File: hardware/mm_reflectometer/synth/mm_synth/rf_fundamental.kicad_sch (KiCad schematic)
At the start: 7 parts

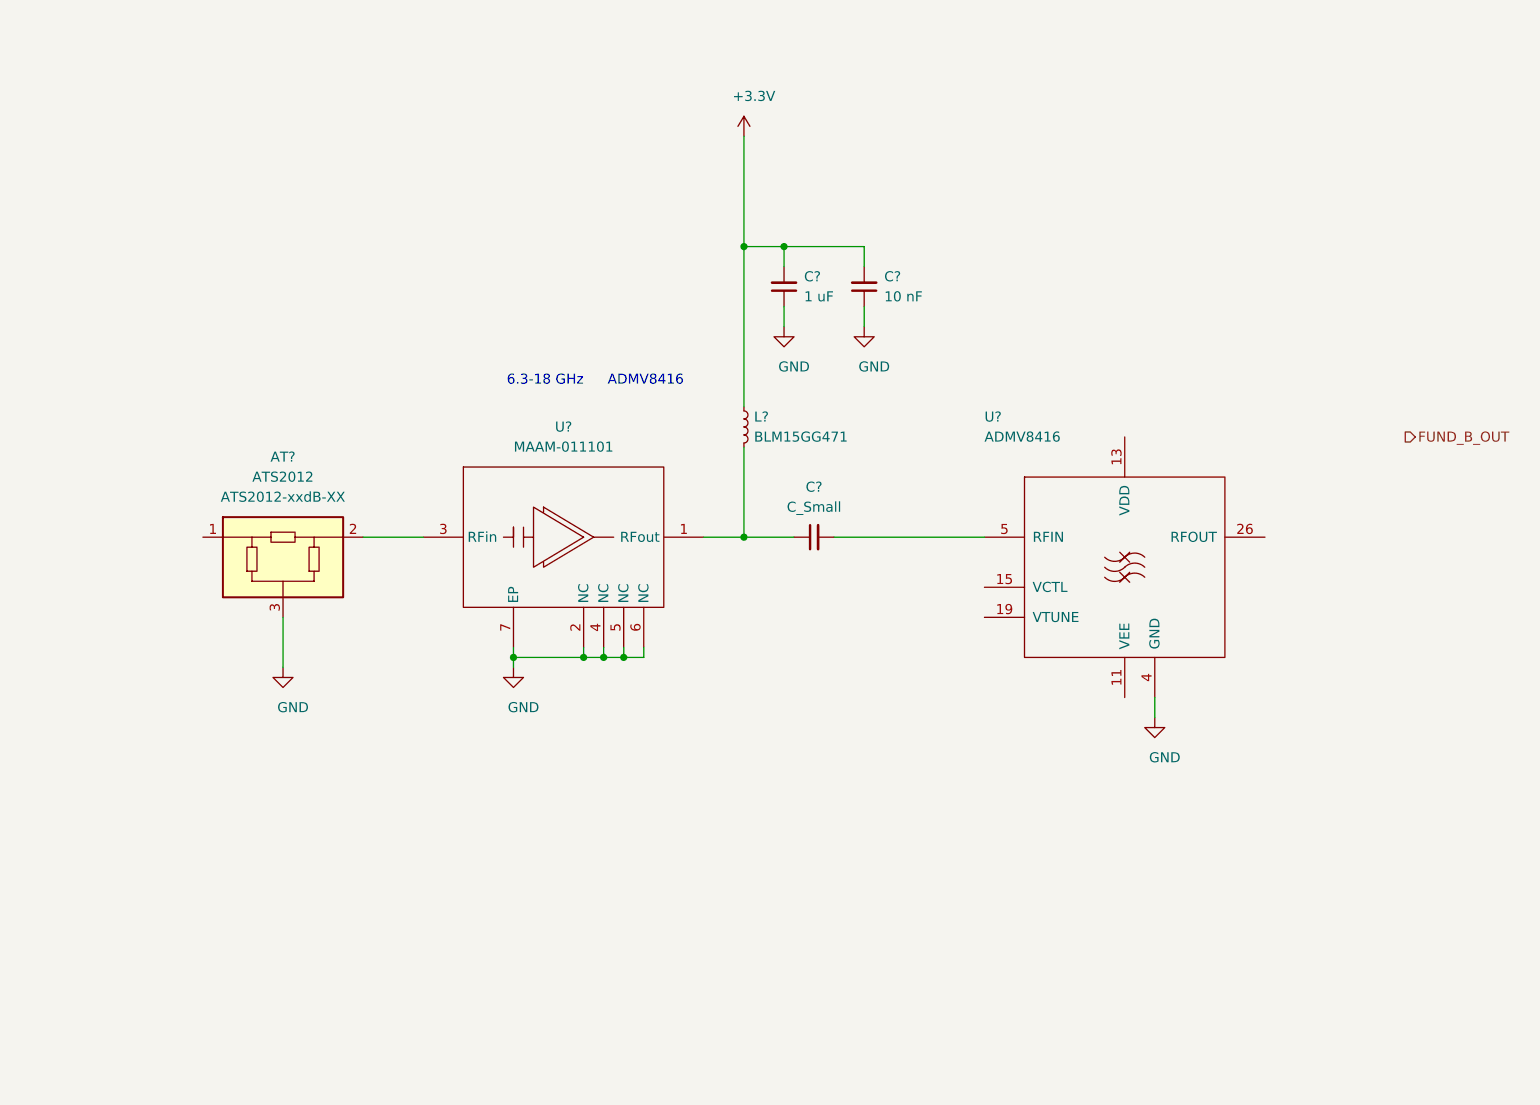
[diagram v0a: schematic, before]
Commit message: adding bias circuitry to mm synth
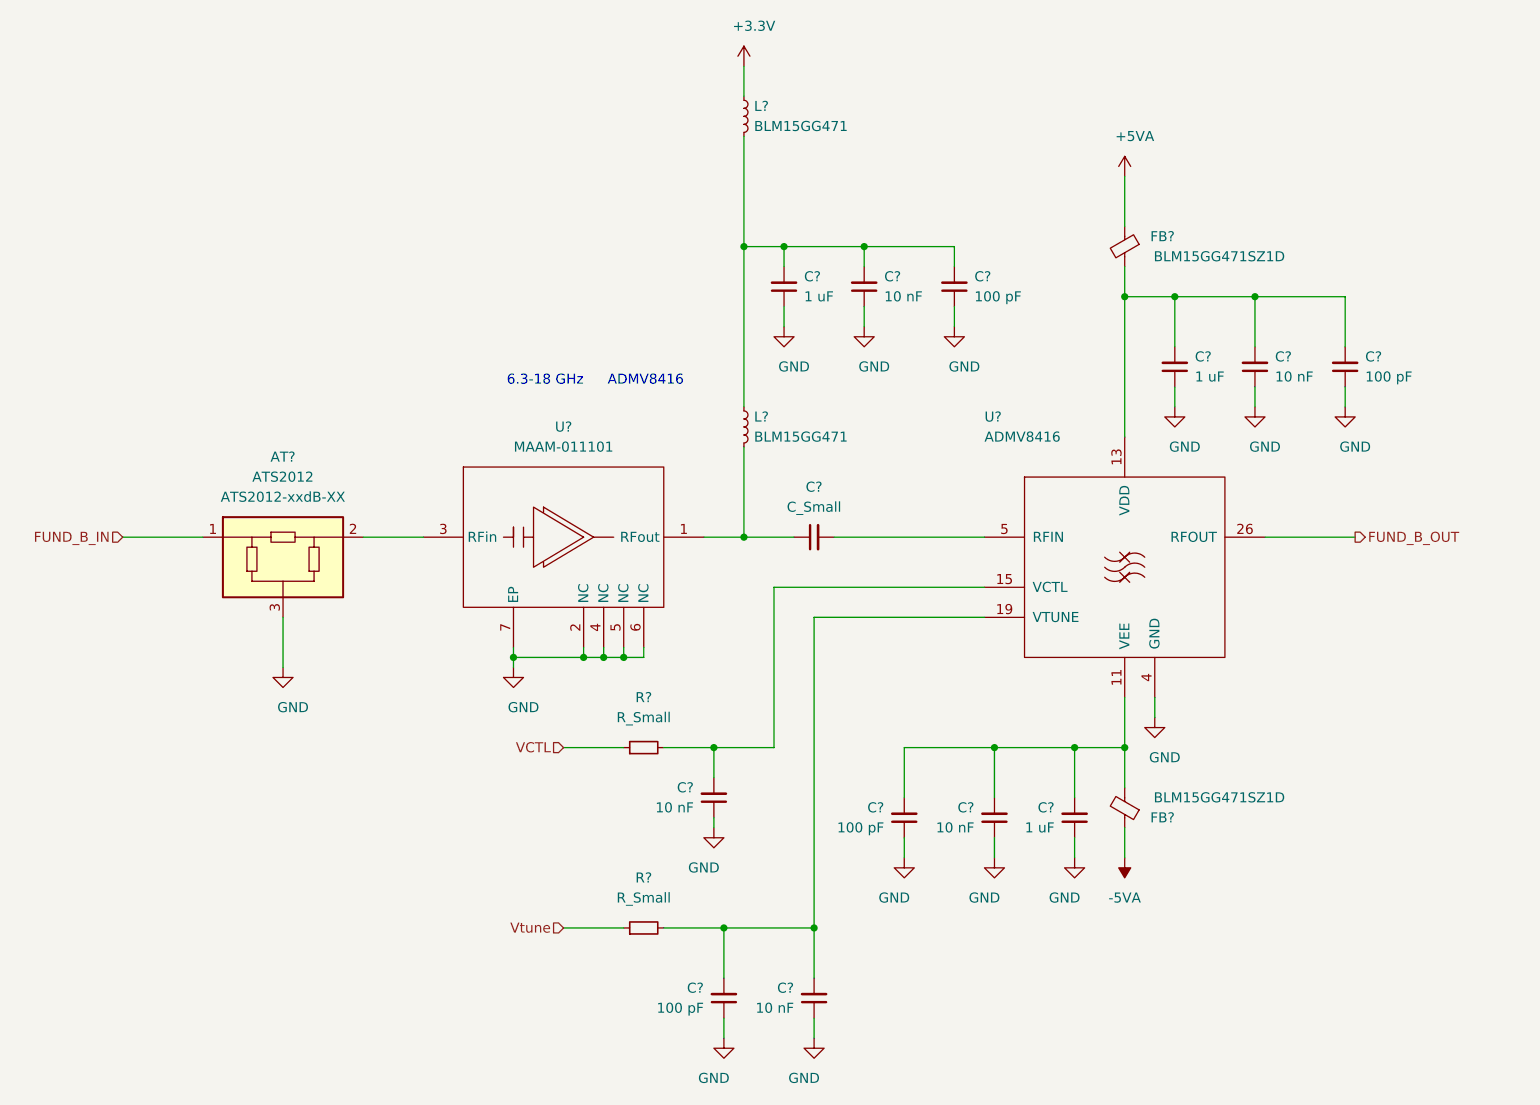
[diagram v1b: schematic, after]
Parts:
- added C? (x4): 10 nF, symbol Device:C_Small
- added C? (x4): 100 pF, symbol Device:C_Small
- added C? (x2): 1 uF, symbol Device:C_Small
- added FB? (x2): BLM15GG471SZ1D, symbol Device:FerriteBead_Small
- added L?: BLM15GG471, symbol Device:L_Small
- added R? (x2): R_Small, symbol Device:R_Small
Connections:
- net +3V3: now also L?.1; no longer C?.2, C?.2, L?.1
- net FUND_B_OUT: now also U?.26 (RFOUT)
- net GND: now also C?.1, C?.1, C?.1, C?.1, C?.1, C?.1, C?.1, C?.1, C?.1, C?.1
- net at U?.11 (VEE): now also C?.2, C?.2, C?.2, FB?.2
- net at U?.13 (VDD): now also C?.2, C?.2, C?.2, FB?.2
- net at U?.15 (VCTL): now also C?.2, R?.2
- net at U?.19 (VTUNE): now also C?.2, C?.2, R?.2
- net FUND_B_IN: now reaches AT?.1
- new net: C?.2, C?.2, C?.2, L?.1, L?.2
- new net +5VA: FB?.1
- new net -5VA: FB?.1
- new net VCTL: R?.1
- new net Vtune: R?.1

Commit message: added dac to mm_synth for vtune/adjstable bias, added ADC for telemetry
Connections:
- net VCTL renamed FILT_VCTL
- net Vtune renamed FILT_Vtune
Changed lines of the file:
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@@
     (effects (font (size 1.27 1.27)) (justify right))
   )
-  (hierarchical_label "VCTL" (shape input) (at 113.03 140.97 180)
+  (hierarchical_label "FILT_VCTL" (shape input) (at 113.03 140.97 180)
     (effects (font (size 1.27 1.27)) (justify right))
   )
-  (hierarchical_label "Vtune" (shape input) (at 113.03 163.83 180)
+  (hierarchical_label "FILT_Vtune" (shape input) (at 113.03 163.83 180)
     (effects (font (size 1.27 1.27)) (justify right))
   )

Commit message: adding digital connections to synth schematic
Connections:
- net +3V3 renamed +3.3VA
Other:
- note added: "0-15V ANALOG"
- note added: "3.3V CMOS"
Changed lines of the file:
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@@
     (stroke (width 0) (type solid) (color 0 0 0 0))
+  )
+  (text "3.3V CMOS" (at 101.6 144.78 0)
+    (effects (font (size 1.27 1.27)) (justify left bottom))
+  )
+  (text "0-15V ANALOG" (at 101.6 167.64 0)
+    (effects (font (size 1.27 1.27)) (justify left bottom))
   )
   (text "6.3-18 GHz" (at 115.57 95.25 180)
@@
     (effects (font (size 1.27 1.27)) (justify left))
   )
-  (symbol (lib_id "power:+3.3V") (at 135.89 54.61 0) (unit 1)
-    (in_bom yes) (on_board yes)
-    (property "Reference" "#PWR0212" (id 0) (at 135.89 58.42 0)
+  (symbol (lib_id "power:+3.3VA") (at 135.89 54.61 0) (unit 1)
+    (in_bom yes) (on_board yes) (fields_autoplaced)
+    (property "Reference" "#PWR?" (id 0) (at 135.89 58.42 0)
       (effects (font (size 1.27 1.27)) hide)
     )
-    (property "Value" "+3.3V" (id 1) (at 137.16 49.53 0))
+    (property "Value" "+3.3VA" (id 1) (at 135.89 50.8 0))
     (property "Footprint" "" (id 2) (at 135.89 54.61 0)
       (effects (font (size 1.27 1.27)) hide)

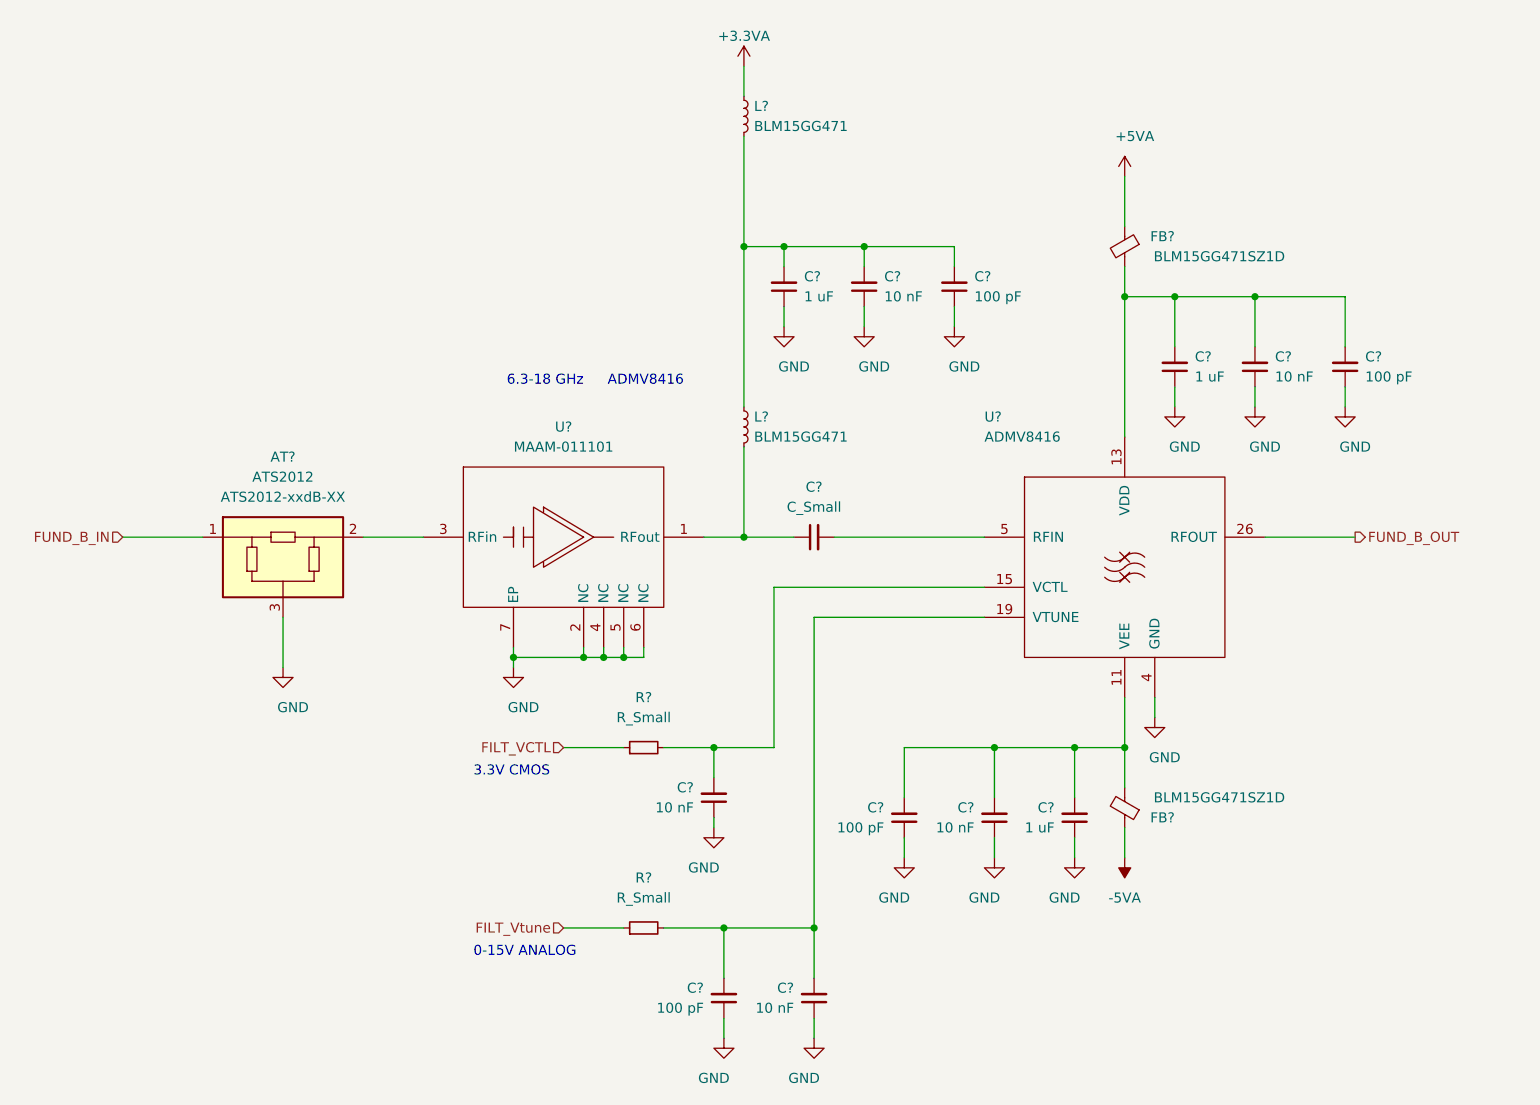
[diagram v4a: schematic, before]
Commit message: work on mm synth schematic - control signals and footprint assignments
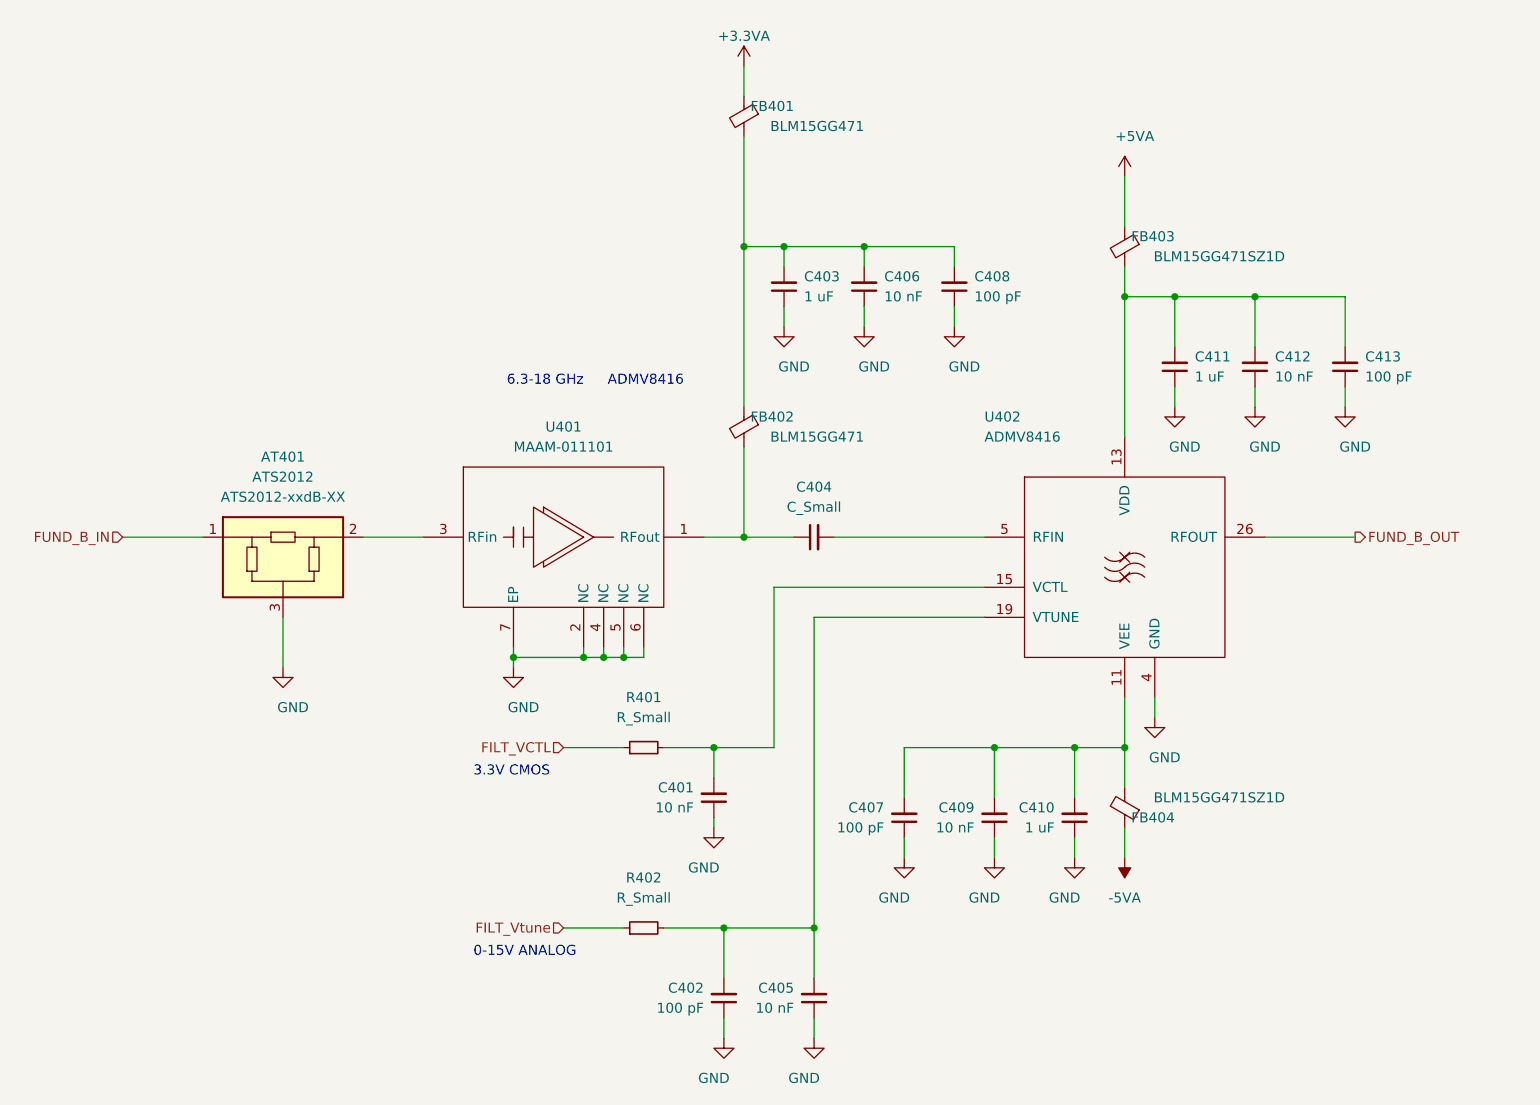
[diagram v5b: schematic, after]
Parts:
- removed L? (x2): BLM15GG471, symbol Device:L_Small
- added FB401, FB402: BLM15GG471, symbol Device:FerriteBead_Small
- C401, C402, C403, C404, C405, C406, C407, C408, C409, C410, C411, C412, C413: renamed from C?; footprint (none) -> Capacitor_SMD:C_0402_1005Metric
- R401, R402: renamed from R?; footprint (none) -> Resistor_SMD:R_0402_1005Metric
- gave numbers to parts that had none: 5
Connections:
- net +3.3VA: now also FB401.1
- net at C403.2, C406.2, C408.2: now also FB401.2, FB402.1
- net at C404.1, U401.1 (RFout): now also FB402.2

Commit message: added aux high speed io connector, fixed hierarchical buses
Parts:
- FB401, FB402: value BLM15GG471 -> BLM15GG471SZ1D; footprint (none) -> Inductor_SMD:L_0402_1005Metric
- FB403, FB404: footprint (none) -> Inductor_SMD:L_0402_1005Metric
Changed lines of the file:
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@@
       (effects (font (size 1.27 1.27)) (justify left))
     )
-    (property "Value" "BLM15GG471" (id 1) (at 151.13 62.23 0)
+    (property "Value" "BLM15GG471SZ1D" (id 1) (at 151.13 62.23 0)
       (effects (font (size 1.27 1.27)) (justify left))
     )
-    (property "Footprint" "" (id 2) (at 137.668 60.96 90)
+    (property "Footprint" "Inductor_SMD:L_0402_1005Metric" (id 2) (at 137.668 60.96 90)
       (effects (font (size 1.27 1.27)) hide)
     )
@@
       (effects (font (size 1.27 1.27)) (justify left))
     )
-    (property "Value" "BLM15GG471" (id 1) (at 151.13 101.6 0)
+    (property "Value" "BLM15GG471SZ1D" (id 1) (at 151.13 101.6 0)
       (effects (font (size 1.27 1.27)) (justify left))
     )
-    (property "Footprint" "" (id 2) (at 137.668 100.33 90)
+    (property "Footprint" "Inductor_SMD:L_0402_1005Metric" (id 2) (at 137.668 100.33 90)
       (effects (font (size 1.27 1.27)) hide)
     )
@@
       (effects (font (size 1.27 1.27)) (justify left))
     )
-    (property "Footprint" "" (id 2) (at 185.928 77.47 90)
+    (property "Footprint" "Inductor_SMD:L_0402_1005Metric" (id 2) (at 185.928 77.47 90)
       (effects (font (size 1.27 1.27)) hide)
     )
@@
       (effects (font (size 1.27 1.27)) (justify left))
     )
-    (property "Footprint" "" (id 2) (at 185.928 148.59 90)
+    (property "Footprint" "Inductor_SMD:L_0402_1005Metric" (id 2) (at 185.928 148.59 90)
       (effects (font (size 1.27 1.27)) hide)
     )

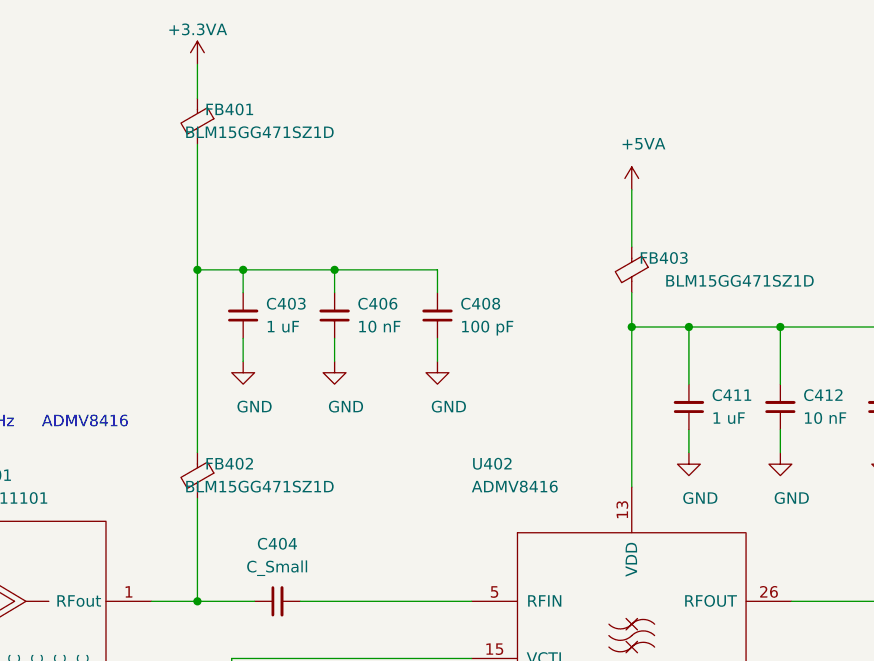
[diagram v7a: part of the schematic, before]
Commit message: added usb PD sink to synth
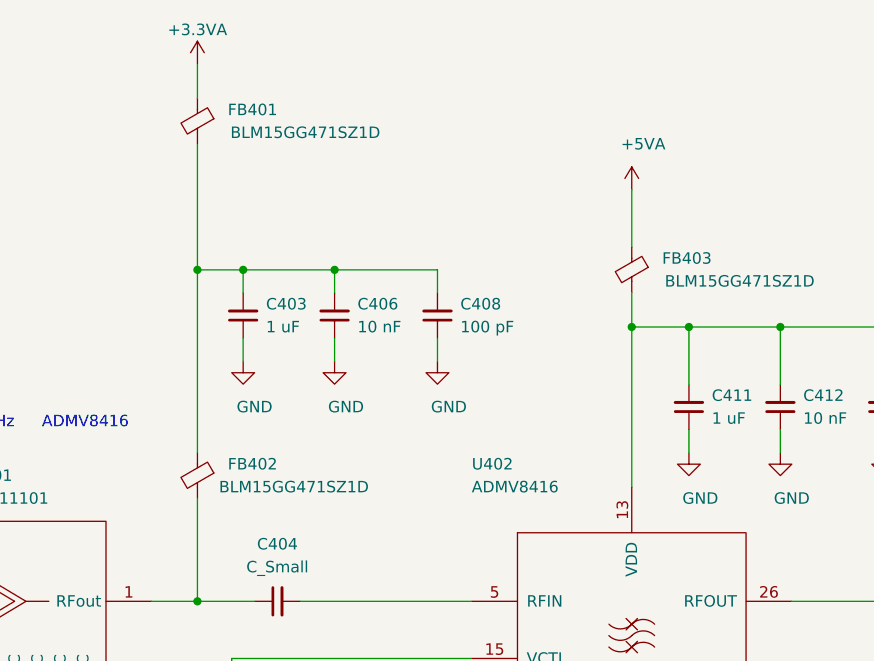
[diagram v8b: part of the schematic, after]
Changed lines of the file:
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@@
   (symbol (lib_id "Device:FerriteBead_Small") (at 135.89 60.96 0) (mirror y) (unit 1)
     (in_bom yes) (on_board yes)
-    (property "Reference" "FB401" (id 0) (at 142.24 59.69 0)
+    (property "Reference" "FB401" (id 0) (at 144.78 59.69 0)
       (effects (font (size 1.27 1.27)) (justify left))
     )
-    (property "Value" "BLM15GG471SZ1D" (id 1) (at 151.13 62.23 0)
+    (property "Value" "BLM15GG471SZ1D" (id 1) (at 156.21 62.23 0)
       (effects (font (size 1.27 1.27)) (justify left))
     )
@@
   (symbol (lib_id "Device:FerriteBead_Small") (at 135.89 100.33 0) (mirror y) (unit 1)
     (in_bom yes) (on_board yes)
-    (property "Reference" "FB402" (id 0) (at 142.24 99.06 0)
+    (property "Reference" "FB402" (id 0) (at 144.78 99.06 0)
       (effects (font (size 1.27 1.27)) (justify left))
     )
-    (property "Value" "BLM15GG471SZ1D" (id 1) (at 151.13 101.6 0)
+    (property "Value" "BLM15GG471SZ1D" (id 1) (at 154.94 101.6 0)
       (effects (font (size 1.27 1.27)) (justify left))
     )
@@
   (symbol (lib_id "Device:FerriteBead_Small") (at 184.15 77.47 0) (mirror y) (unit 1)
     (in_bom yes) (on_board yes)
-    (property "Reference" "FB403" (id 0) (at 190.5 76.2 0)
+    (property "Reference" "FB403" (id 0) (at 193.04 76.2 0)
       (effects (font (size 1.27 1.27)) (justify left))
     )
